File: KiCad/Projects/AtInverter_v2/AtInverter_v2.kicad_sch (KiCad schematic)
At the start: 115 parts, among them Q1 IRFB4020PBF, Q2 IRFB4020PBF, Q3 IRFB4020PBF, Q4 IRFB4020PBF, T1 ZMPT101B, U1 LM358N, U10 TLV61046ADB, U11 R-78HE5.0-0.3, U2 74LVC1G32, U3 LM393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

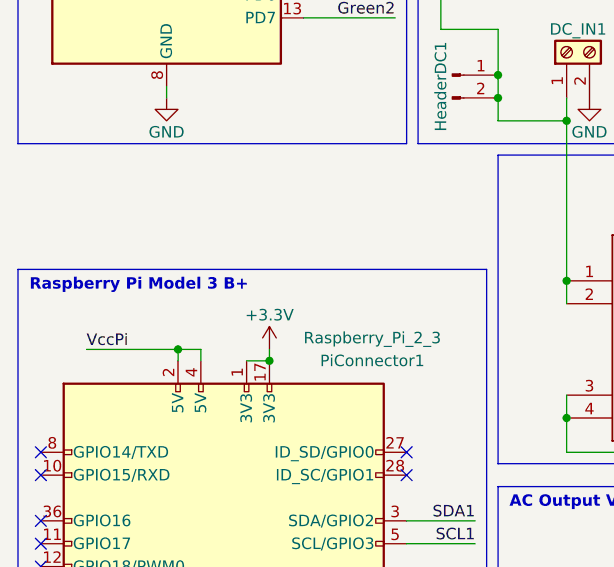
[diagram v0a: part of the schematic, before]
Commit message: Editted pin mapping in class, modified blink code, fully functioning
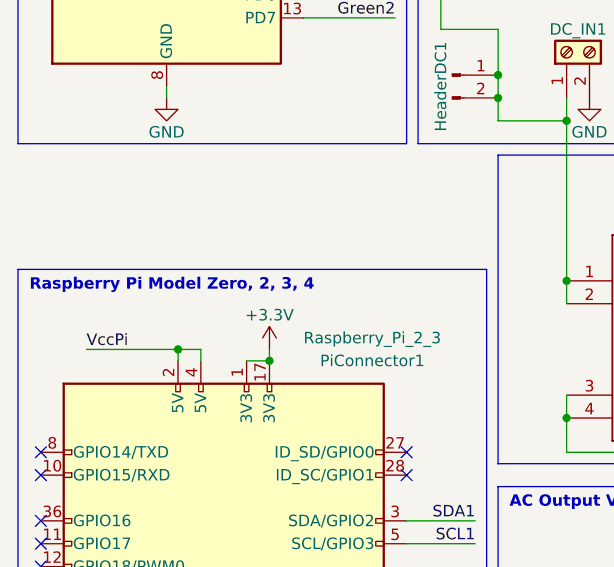
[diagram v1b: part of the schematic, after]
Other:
- note added: "Raspberry Pi Model Zero, 2, 3, 4"
- note removed: "Raspberry Pi Model 3 B+"
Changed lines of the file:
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@@
 		)
 	)
-	(text "Raspberry Pi Model 3 B+"
+	(text "Raspberry Pi Model Zero, 2, 3, 4 "
 		(exclude_from_sim no)
 		(at 13.97 120.65 0)

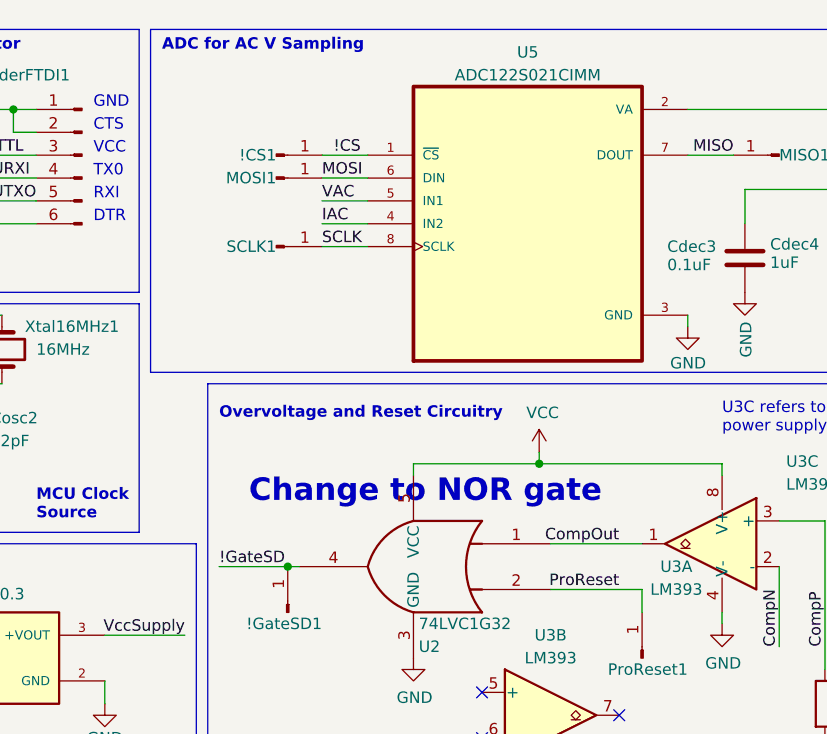
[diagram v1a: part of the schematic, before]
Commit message: ZMPT101B lib fix
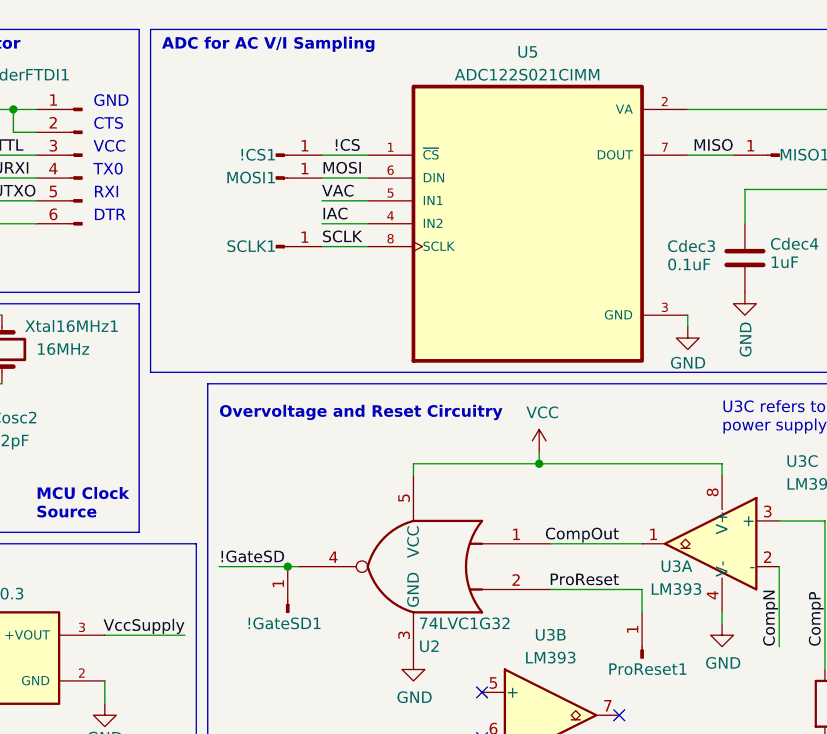
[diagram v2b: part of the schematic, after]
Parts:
- U2: symbol 74xGxx:74LVC1G32 -> 74xGxx:74AHC1G02
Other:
- note added: "ADC for AC V/I Sampling"
- note removed: "ADC for AC V Sampling"
- note removed: "Change to NOR gate"
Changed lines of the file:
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@@
 		)
 	)
-	(text "ADC for AC V Sampling"
+	(text "ADC for AC V/I Sampling"
 		(exclude_from_sim no)
 		(at 96.52 15.24 0)
@@
 		)
 	)
-	(text "Change to NOR gate"
-		(exclude_from_sim no)
-		(at 106.172 65.532 0)
-		(effects
-			(font
-				(size 2.5 2.5)
-				(thickness 0.254)
-				(bold yes)
-			)
-			(justify left bottom)
-		)
-	)
 	(text "Power Supply Network"
 		(exclude_from_sim no)
@@
 	)
 	(symbol
-		(lib_id "74xGxx:74LVC1G32")
+		(lib_id "74xGxx:74AHC1G02")
 		(at 124.46 72.39 0)
 		(mirror y)

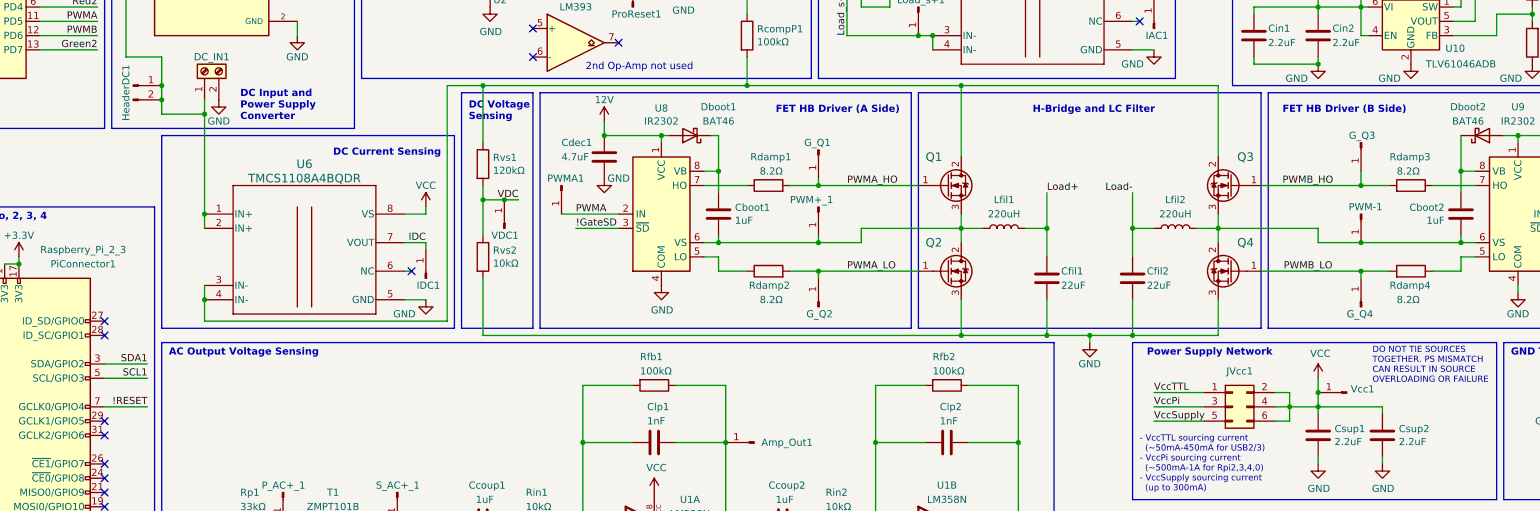
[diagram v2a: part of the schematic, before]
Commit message: Added dedicated section for hardware description and high level diagrams
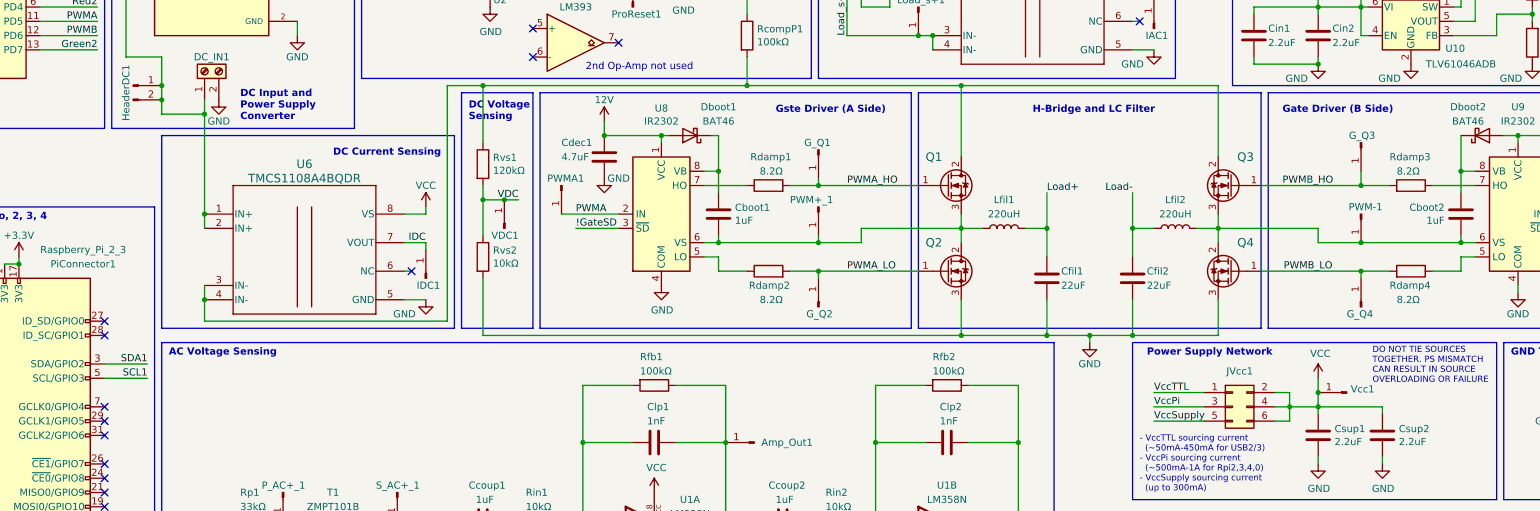
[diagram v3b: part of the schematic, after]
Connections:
- net !RESET: no longer PiConnector1.7 (GCLK0/GPIO4)
- no-connect marks 36 -> 37
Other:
- note added: "AC Voltage Sensing"
- note added: "Gate Driver (B Side)"
- note added: "Gste Driver (A Side)"
- note removed: "AC Output Voltage Sensing"
- note removed: "FET HB Driver (A Side)"
- note removed: "FET HB Driver (B Side)"
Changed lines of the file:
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@@
 	)
 	(no_connect
+		(at 55.88 153.67)
+	)
+	(no_connect
 		(at 55.88 158.75)
 	)
@@
 	(wire
 		(pts
-			(xy 55.88 153.67) (xy 63.5 153.67)
-		)
-		(stroke
-			(width 0)
-			(type default)
-		)
-	)
-	(wire
-		(pts
 			(xy 283.21 162.56) (xy 283.21 163.83)
 		)
@@
 		)
 	)
-	(text "AC Output Voltage Sensing"
+	(text "AC Voltage Sensing"
 		(exclude_from_sim no)
 		(at 67.31 144.78 0)
@@
 		)
 	)
-	(text "FET HB Driver (B Side)"
+	(text "Gate Driver (B Side)"
 		(exclude_from_sim no)
 		(at 265.43 101.6 0)
@@
 		)
 	)
-	(text "FET HB Driver (A Side)"
+	(text "Gste Driver (A Side)"
 		(exclude_from_sim no)
 		(at 175.26 101.6 0)
@@
 		(effects
 			(font
-				(size 1.27 1.27)
-			)
-			(justify right bottom)
-		)
-	)
-	(label "!RESET"
-		(at 63.5 153.67 180)
-		(effects
-			(font

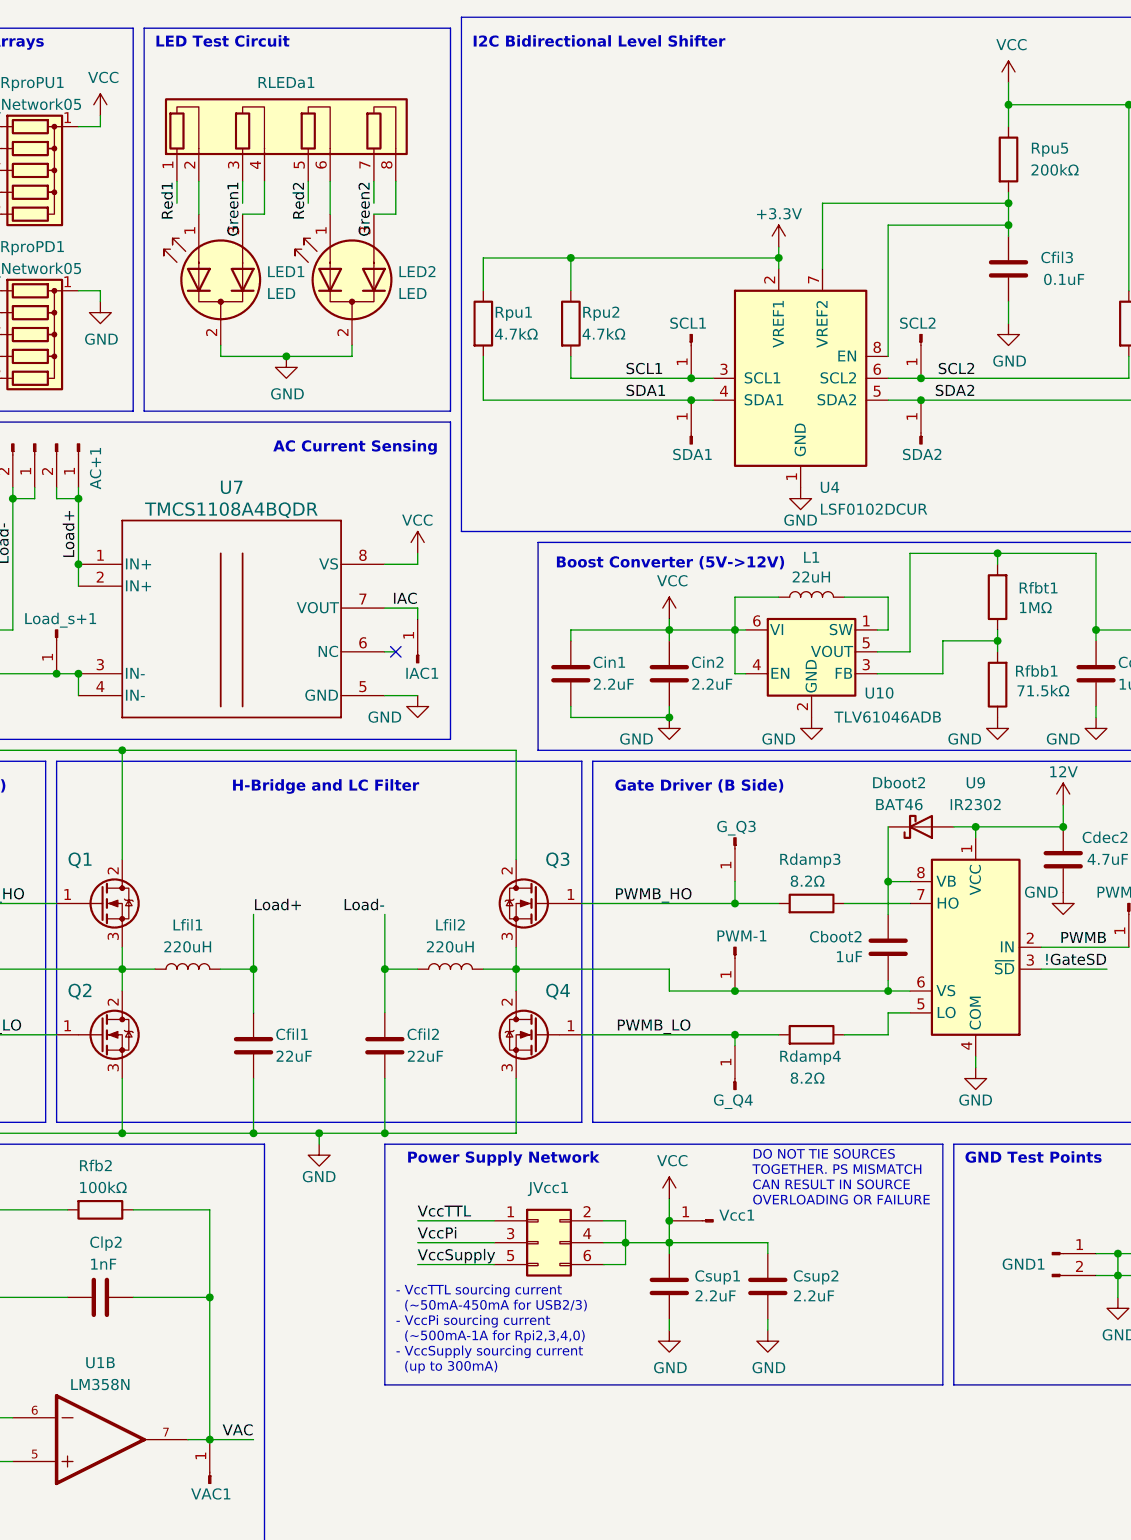
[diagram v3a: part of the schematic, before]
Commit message: modifications to a_v2 hardware docs section
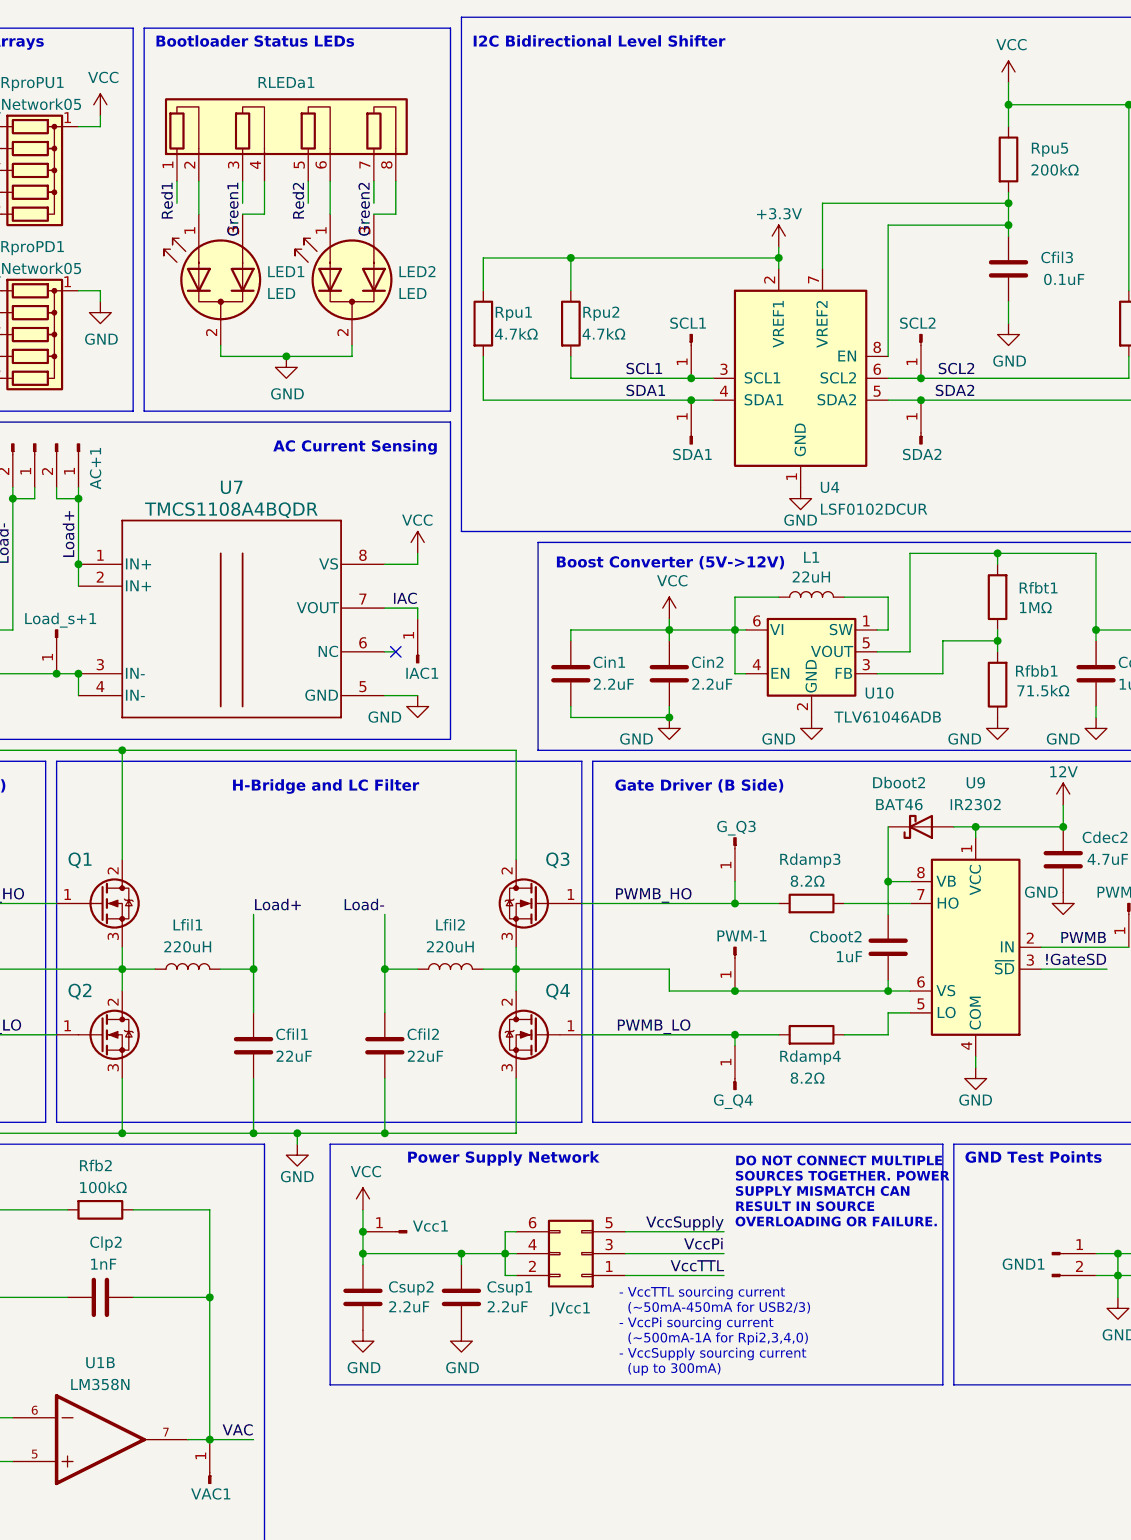
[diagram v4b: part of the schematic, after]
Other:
- note added: "Bootloader Status LEDs"
- note added: "DO NOT CONNECT MULTIPLE SOURCES TOGETHER. POWER SUPPLY MISMATCH CAN RESULT IN SOURCE OVERLOADING OR FAILURE."
- note removed: "DO NOT TIE SOURCES TOGETHER. PS MISMATCH CAN RESULT IN SOURCE OVERLOADING OR FAILURE"
- note removed: "LED Test Circuit"

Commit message: Blink and DC V/I software documentation complete
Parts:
- Rs1: value 100Ω -> 6.8Ω
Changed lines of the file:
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@@
 			)
 		)
-		(property "Value" "100Ω"
+		(property "Value" "6.8Ω"
 			(at 123.19 180.34 0)
 			(effects

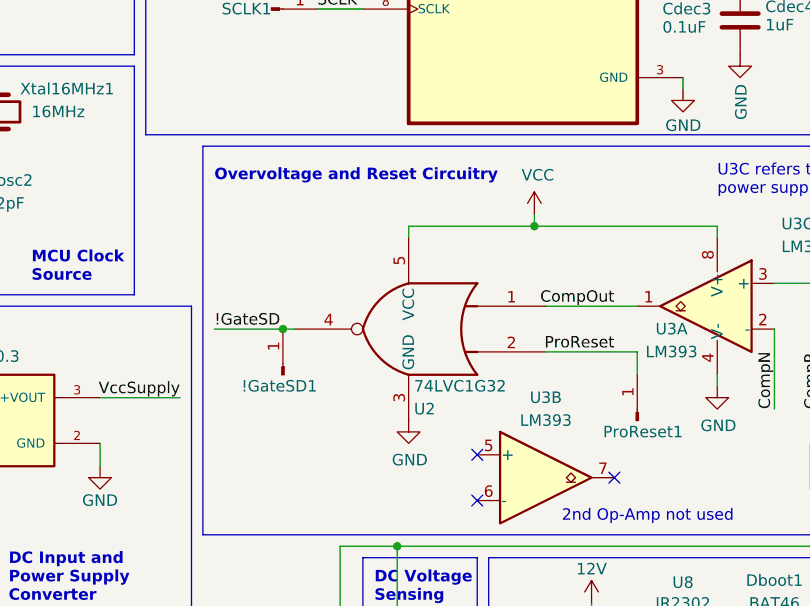
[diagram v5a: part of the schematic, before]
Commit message: Completed Overvoltage and Reset Protection Hardware Section
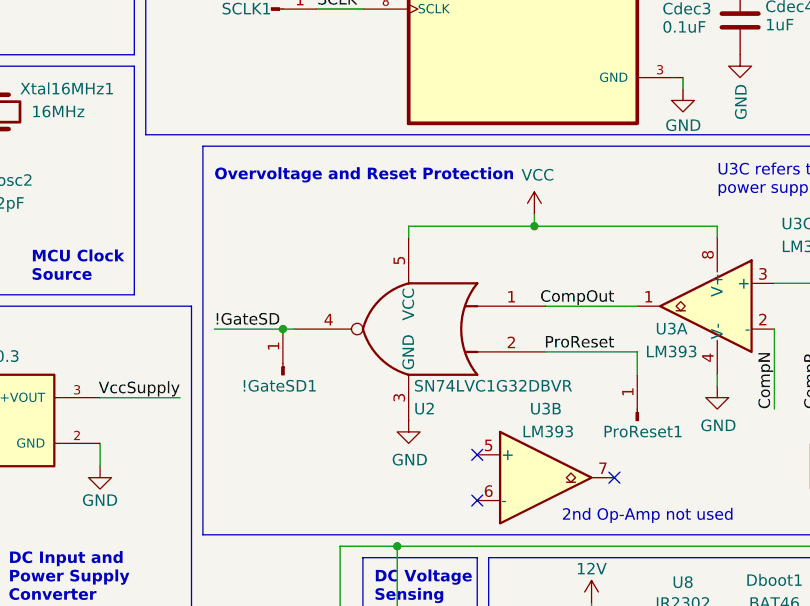
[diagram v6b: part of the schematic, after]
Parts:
- U2: value 74LVC1G32 -> SN74LVC1G32DBVR
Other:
- note added: "Overvoltage and Reset Protection"
- note removed: "Overvoltage and Reset Circuitry"
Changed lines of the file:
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@@
 		)
 	)
-	(text "Overvoltage and Reset Circuitry"
+	(text "Overvoltage and Reset Protection"
 		(exclude_from_sim no)
 		(at 102.87 56.134 0)
@@
 		(dnp no)
 		(property "Reference" "U3"
-			(at 139.7 80.01 0)
+			(at 139.7 81.28 0)
 			(effects
 				(font
@@
 		)
 		(property "Value" "LM393"
-			(at 139.7 82.55 0)
+			(at 139.954 83.82 0)
 			(effects
 				(font
@@
 			)
 		)
-		(property "Value" "74LVC1G32"
+		(property "Value" "SN74LVC1G32DBVR"
 			(at 125.0441 78.74 0)
 			(effects
